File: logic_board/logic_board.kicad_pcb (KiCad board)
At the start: 4 copper layers, 80 x 30 mm, 56 parts, among them J1 SWD, J2 Audio In, J3 SJ2-3595X-SMT, J4 Amphenol 124015, J5 Batt, J6 Serial, SW1 TL3315NF160Q, SW2 TL3315NF160Q, SW3 TL3315NF160Q, SW4 TL3315NF160Q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

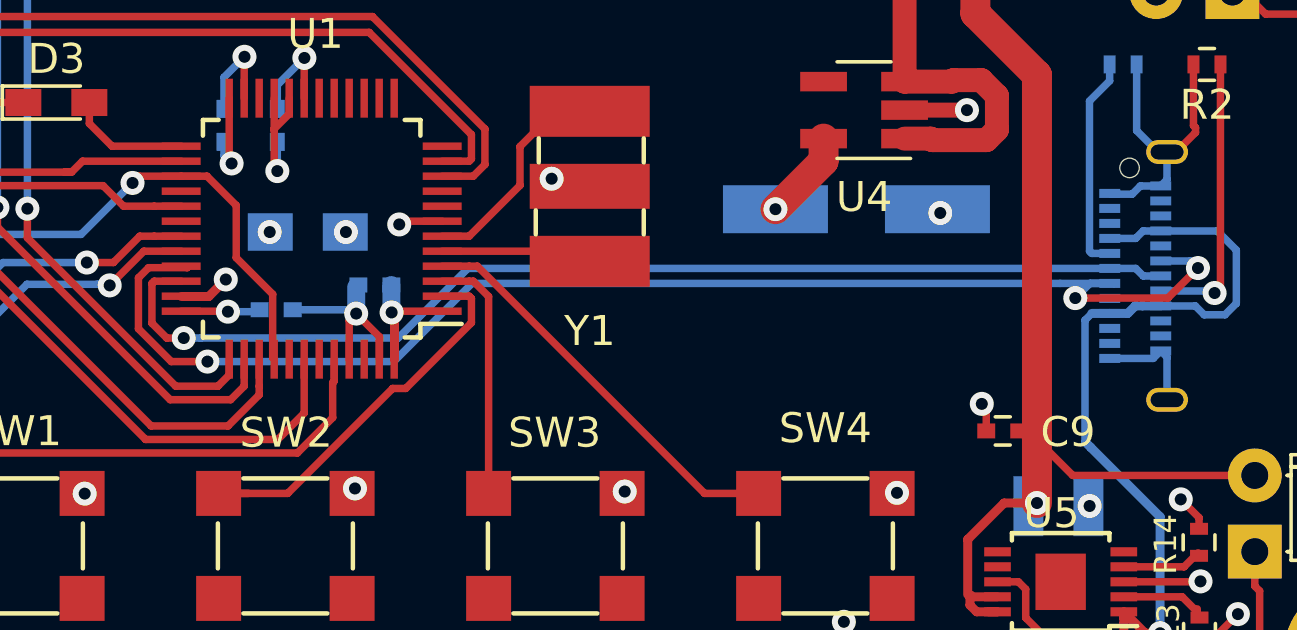
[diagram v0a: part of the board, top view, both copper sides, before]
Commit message: Route USB data lines away from MCU resonator
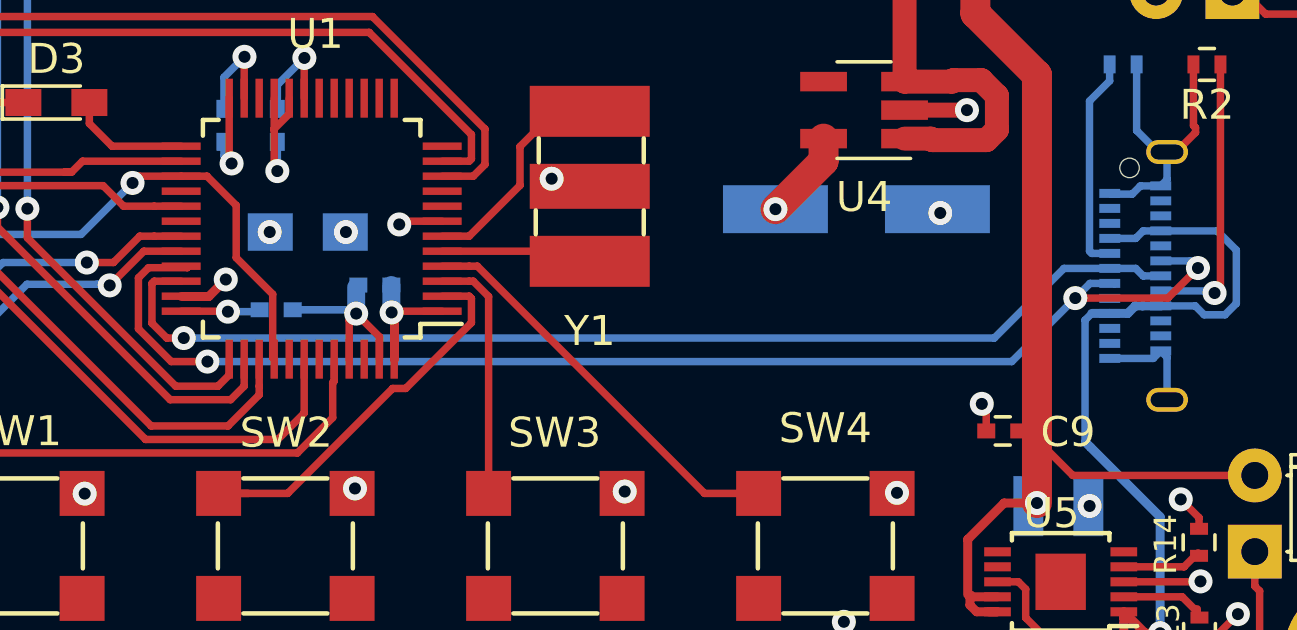
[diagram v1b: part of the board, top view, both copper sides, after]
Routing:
- net USB_DM: track 44.7 -> 43.3 mm
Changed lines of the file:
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@@
     (thickness 1.6)
     (drawings 21)
-    (tracks 512)
+    (tracks 509)
     (zones 0)
     (modules 56)
@@
   (gr_line (start 180 102.5) (end 180 127.5) (layer Edge.Cuts) (width 0.05))
   (gr_line (start 102.5 100) (end 113 100) (layer Edge.Cuts) (width 0.05))
-  (via (at 163.83 112.903) (size 0.8) (drill 0.4) (layers F.Cu B.Cu) (net 2))
   (via (at 141.478 113.538) (size 0.8) (drill 0.4) (layers F.Cu B.Cu) (net 1))
   (via (at 119.3419 116.8654) (size 0.8) (drill 0.4) (layers F.Cu B.Cu) (net 1))
@@
   (segment (start 159.94 111.172) (end 158.336 112.776) (width 1) (layer F.Cu) (net 1))
   (segment (start 159.94 110.424) (end 159.94 111.172) (width 1) (layer F.Cu) (net 1))
+  (via (at 163.83 112.903) (size 0.8) (drill 0.4) (layers F.Cu B.Cu) (net 2))
   (via (at 150.876 111.76) (size 0.8) (drill 0.4) (layers F.Cu B.Cu) (net 2))
   (via (at 144.018 113.538) (size 0.8) (drill 0.4) (layers F.Cu B.Cu) (net 2))
@@
   (segment (start 169.48 115.25) (end 168.820014 115.25) (width 0.25) (layer B.Cu) (net 24))
   (segment (start 169.606 115.25) (end 169.630999 115.274999) (width 0.25) (layer B.Cu) (net 24))
-  (segment (start 167.828 115.25) (end 169.606 115.25) (width 0.25) (layer B.Cu) (net 24))
   (via (at 172.419299 114.737949) (size 0.8) (drill 0.4) (layers F.Cu B.Cu) (net 24))
   (segment (start 171.418321 115.738927) (end 172.419299 114.737949) (width 0.25) (layer F.Cu) (net 24))
@@
   (segment (start 172.18135 114.5) (end 171.18 114.5) (width 0.25) (layer B.Cu) (net 24))
   (segment (start 172.419299 114.737949) (end 172.18135 114.5) (width 0.25) (layer B.Cu) (net 24))
-  (segment (start 167.828 115.25) (end 148.219112 115.25) (width 0.25) (layer B.Cu) (net 24))
-  (segment (start 145.613112 117.856) (end 139.402538 117.856) (width 0.25) (layer B.Cu) (net 24))
   (via (at 139.402538 117.856) (size 0.8) (drill 0.4) (layers F.Cu B.Cu) (net 24))
-  (segment (start 148.219112 115.25) (end 145.613112 117.856) (width 0.25) (layer B.Cu) (net 24))
   (segment (start 138.72923 114.72623) (end 138.729239 114.726239) (width 0.25) (layer F.Cu) (net 24))
   (segment (start 137.102529 116.762884) (end 137.10253 115.06484) (width 0.25) (layer F.Cu) (net 24))
@@
   (segment (start 138.195645 117.856) (end 137.102529 116.762884) (width 0.25) (layer F.Cu) (net 24))
   (segment (start 139.402538 117.856) (end 138.195645 117.856) (width 0.25) (layer F.Cu) (net 24))
+  (segment (start 166.214014 117.856) (end 168.331087 115.738927) (width 0.25) (layer B.Cu) (net 24))
+  (segment (start 139.402538 117.856) (end 166.214014 117.856) (width 0.25) (layer B.Cu) (net 24))
   (segment (start 170.594998 115) (end 171.18 115) (width 0.25) (layer B.Cu) (net 25))
   (segment (start 170.344998 114.75) (end 170.594998 115) (width 0.25) (layer B.Cu) (net 25))
@@
   (segment (start 138.047195 117.07114) (end 137.552539 116.576484) (width 0.25) (layer F.Cu) (net 25))
   (segment (start 138.61288 117.07114) (end 138.047195 117.07114) (width 0.25) (layer F.Cu) (net 25))
-  (segment (start 145.761562 117.07114) (end 139.178565 117.07114) (width 0.25) (layer B.Cu) (net 25))
-  (segment (start 139.178565 117.07114) (end 138.61288 117.07114) (width 0.25) (layer B.Cu) (net 25))
-  (segment (start 148.082702 114.75) (end 145.761562 117.07114) (width 0.25) (layer B.Cu) (net 25))
-  (segment (start 169.48 114.75) (end 148.082702 114.75) (width 0.25) (layer B.Cu) (net 25))
+  (segment (start 167.952 114.75) (end 169.48 114.75) (width 0.25) (layer B.Cu) (net 25))
+  (segment (start 165.63086 117.07114) (end 167.952 114.75) (width 0.25) (layer B.Cu) (net 25))
+  (segment (start 138.61288 117.07114) (end 165.63086 117.07114) (width 0.25) (layer B.Cu) (net 25))
   (segment (start 172.397 126.0999) (end 172.397 126.1999) (width 0.25) (layer F.Cu) (net 26))
   (segment (start 169.9482 125.6966) (end 171.8937 125.6966) (width 0.25) (layer F.Cu) (net 26))

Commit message: Adjust DRC rules
Change minimum trace clearance to 0.127mm (5 mil), which is specified by OSHPark. This silences
a bunch of DRC warnings around the charger IC footprint.
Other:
- net class Default: clearance 0.2 -> 0.127
- rule trace_clearance: 0.2 -> 0.127
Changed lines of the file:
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@@
-(kicad_pcb (version 20171130) (host pcbnew "(5.1.0-0)")
+(kicad_pcb (version 20171130) (host pcbnew "(5.1.5-0-10_14)")
   (general
     (thickness 1.6)
@@
     (user_trace_width 1.25)
     (user_trace_width 1.5)
-    (trace_clearance 0.2)
+    (trace_clearance 0.127)
     (zone_clearance 0.508)
     (zone_45_only no)
@@
     (pad_drill 0.9)
     (pad_to_mask_clearance 0.0508)
-    (solder_mask_min_width 0.101)
     (aux_axis_origin 0 0)
     (visible_elements FFFDFF7F)
@@
   (net 70 "Net-(U4-Pad4)")
   (net_class Default "This is the default net class."
-    (clearance 0.2)
+    (clearance 0.127)
     (trace_width 0.25)
     (via_dia 0.8)

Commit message: Move vias off pads
Having a via on a pad can complicate soldering because the vias wick away
solder.
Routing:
- net GND: track 61.8 -> 85.9 mm, vias 33 -> 31
- net +3V3: track 31.8 -> 41.2 mm, vias 13 -> 12
- net Net-(C23-Pad1): track 19.6 -> 23.3 mm
- net +BATT: track 34.8 -> 35.7 mm

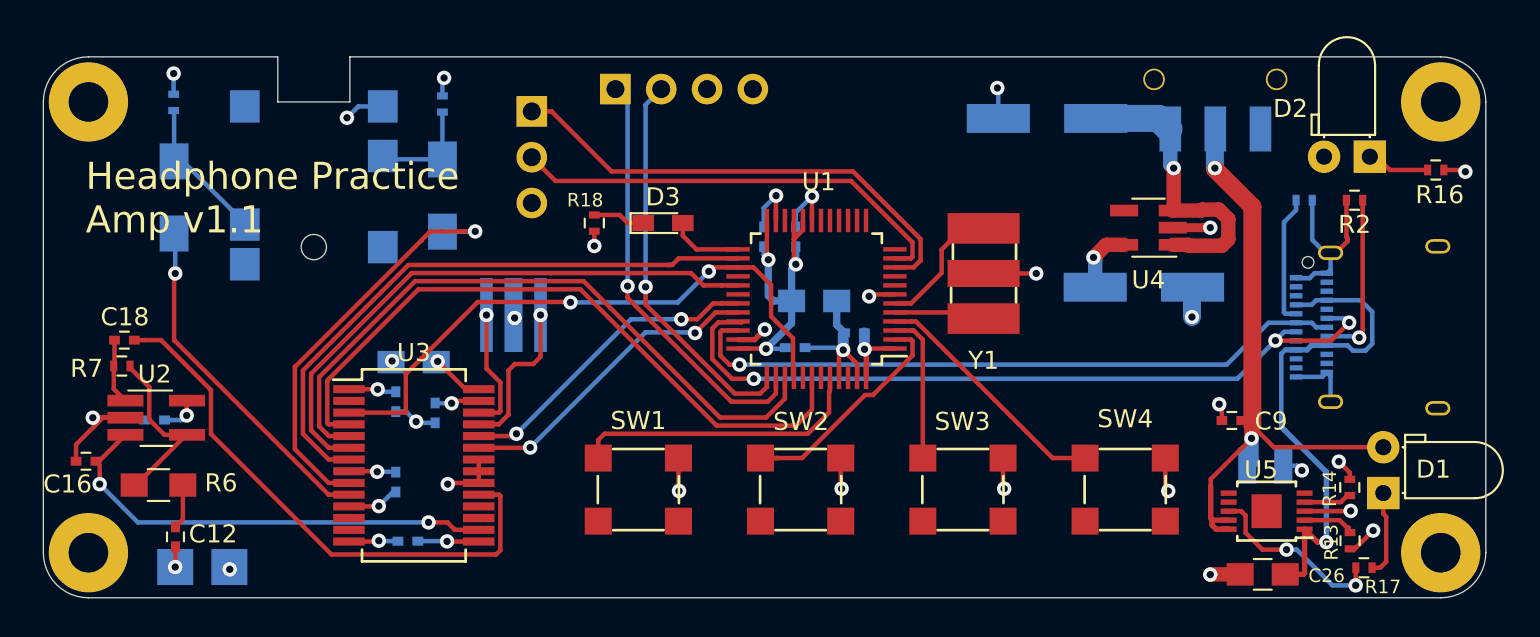
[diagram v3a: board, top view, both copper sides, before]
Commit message: A little more board cleanup
Move some vias off pads that I missed in the last change.
Clean up silk screened references.
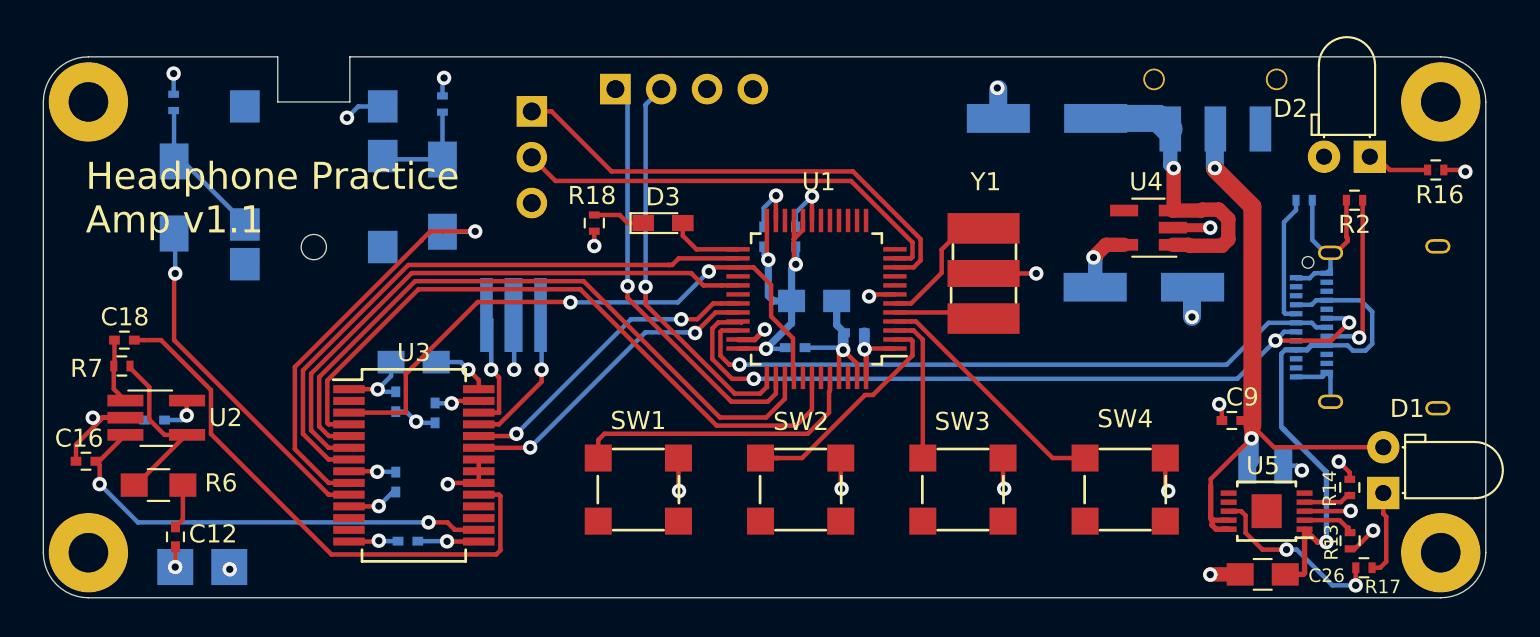
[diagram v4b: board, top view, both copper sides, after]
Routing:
- net GND: track 85.9 -> 89.3 mm
- net +3V3: track 41.2 -> 43.1 mm, vias 12 -> 11
- net Net-(U3-Pad25): track 8.73 -> 8.19 mm

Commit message: Move a bunch of bypass caps to the top of the board.
There is a lot of lore around bypass caps. I suspect it probably
doesn't matter much, but this is the more conservative approach.
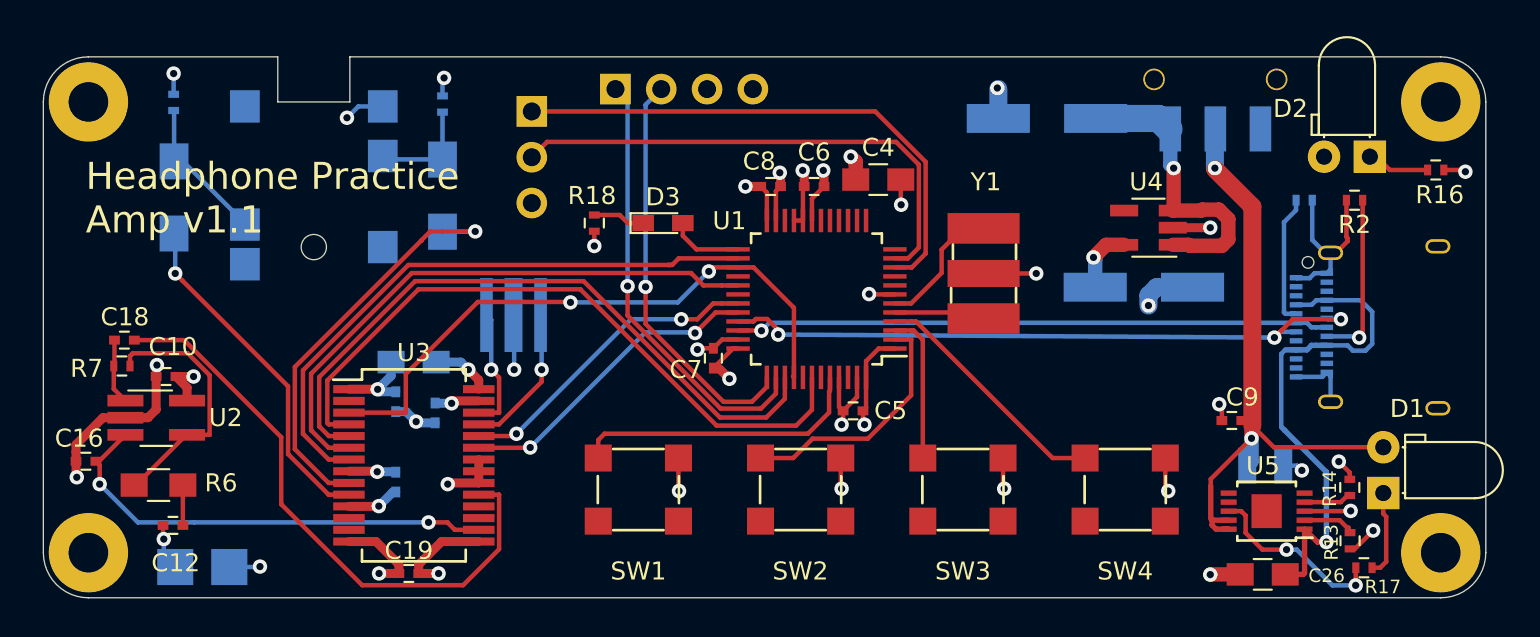
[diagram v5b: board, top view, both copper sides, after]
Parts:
- C10, C19, C4, C5, C6, C7, C8: moved to F.Cu
- moved C4 7.61 mm to (146.3, 106.8)
- moved C7 4.57 mm to (137.2, 116.7), turned to 90 degrees
- moved C5 4.33 mm to (144.9, 119.6)
- moved C6 2.97 mm to (142.7, 107.2), turned to 0 degrees
- moved C8 2.82 mm to (140.3, 107.2), turned to 0 degrees
- moved C10 2.50 mm to (106.8, 117.7)
- moved C19 1.79 mm to (120.3, 128.7)
- moved C12 0.65 mm to (107.2, 126.0), turned to 180 degrees
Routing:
- net USB_DM: track 43.3 -> 36.6 mm
- net +3V3: track 43.1 -> 38.6 mm, vias 11 -> 12
- net Net-(R6-Pad1): track 9.95 -> 14.3 mm
- net USB_DP: track 37.2 -> 32.9 mm
- net Net-(J6-Pad2): track 24.9 -> 28.5 mm
- net GND: track 89.3 -> 92.6 mm, vias 31 -> 33
- net Net-(J6-Pad1): track 27.3 -> 30.1 mm
- net Net-(C18-Pad2): track 31.0 -> 33.0 mm
- net Net-(C12-Pad2): track 1.13 -> 2.59 mm
- net Net-(J1-Pad2): track 21.8 -> 22.8 mm
- net Net-(J1-Pad1): track 23.6 -> 24.4 mm

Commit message: Nitpicky routing cleanup
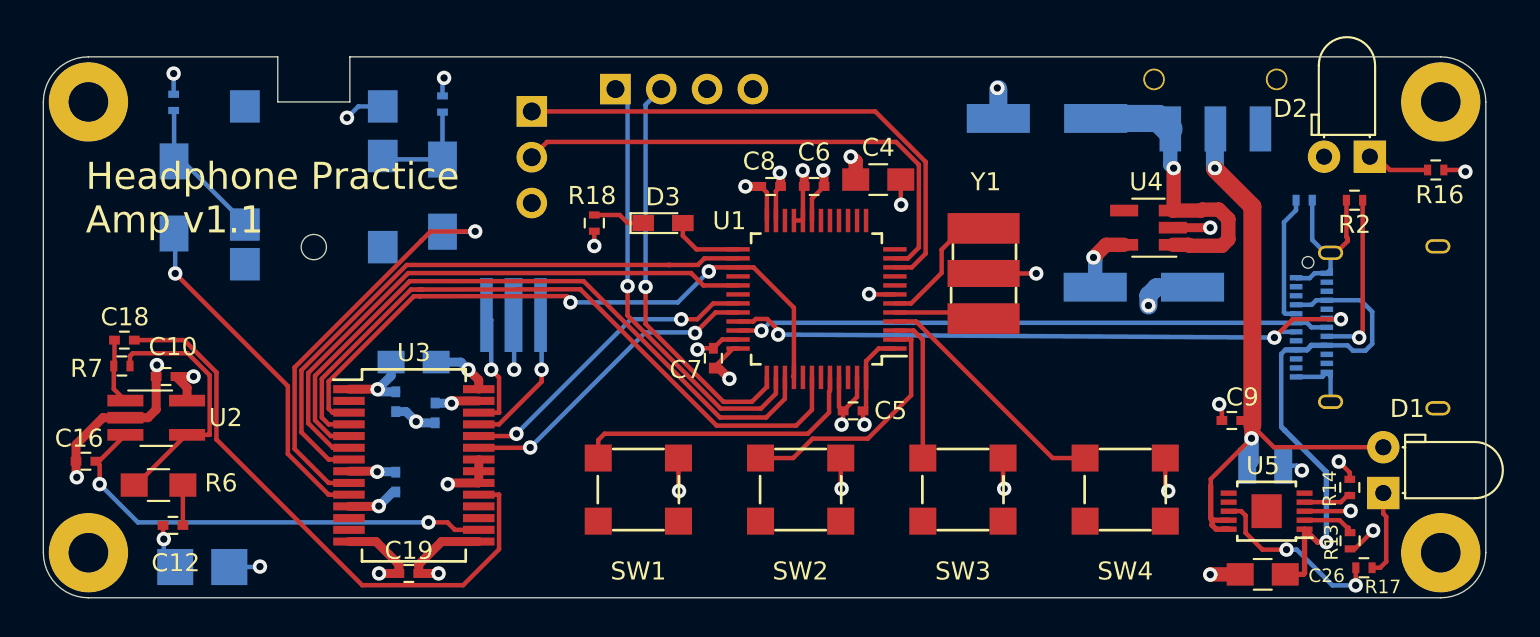
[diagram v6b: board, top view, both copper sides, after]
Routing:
- net BCLK: track 34.2 -> 36.4 mm
- net DACDAT: track 37.9 -> 38.6 mm

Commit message: Consolidate UART and SWD headers into a single one, which takes up less space.
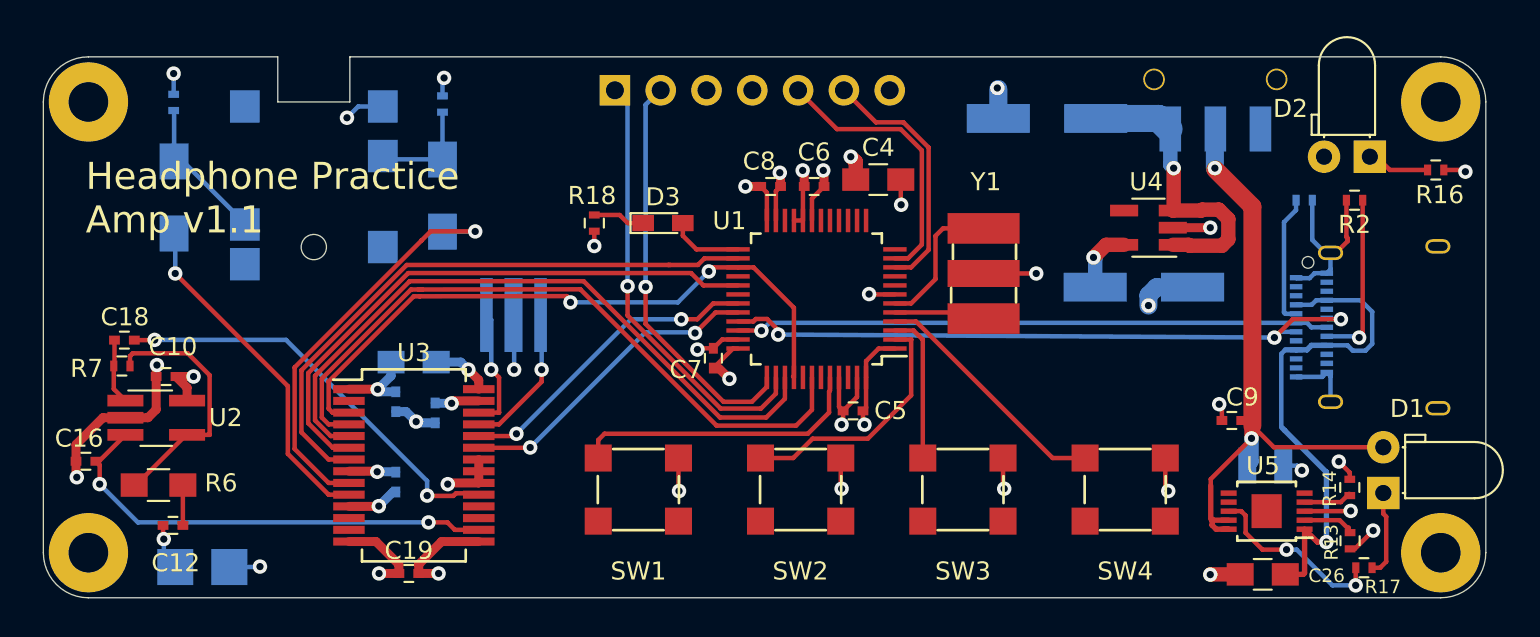
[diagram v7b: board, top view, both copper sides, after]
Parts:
- removed J6: Serial, Pin_Headers:Pin_Header_Straight_1x03_Pitch2.54mm
- J1: value SWD -> Debug; footprint Pin_Headers:Pin_Header_Straight_1x04_Pitch2.54mm -> Pin_Headers:Pin_Header_Straight_1x07_Pitch2.54mm
- moved J1 0.07 mm to (131.7, 101.9)
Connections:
- U1 pad 10: Net-(J6-Pad1) -> Net-(J1-Pad6)
- U1 pad 11: Net-(J6-Pad2) -> Net-(J1-Pad5)
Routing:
- net Net-(J6-Pad1): track 30.1 -> 0.00 mm
- net Net-(J6-Pad2): track 28.5 -> 0.00 mm
- net Net-(J1-Pad5): track 0.00 -> 15.3 mm
- net Net-(J1-Pad6): track 0.00 -> 14.0 mm
- net Net-(C18-Pad2): track 33.0 -> 23.3 mm, vias 0 -> 2
- net Net-(U1-Pad6): track 7.40 -> 8.04 mm
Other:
- board text added: "SRX"
- board text added: "STX"
- board text removed: "RX"
- board text removed: "TX"
